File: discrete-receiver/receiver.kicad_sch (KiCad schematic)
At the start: 75 parts, among them J1 His Excellence, J7 Her Excellency, T1 H1102NLT, T2 MABA-007159-000000, U1 SN74CBT3253DBQR, U16 PSA4-5043_, U18 SN74LVC1G3157DBVR, U2 OPA1612AxD, U3 OPA1612AxD, U5 ADE-12+

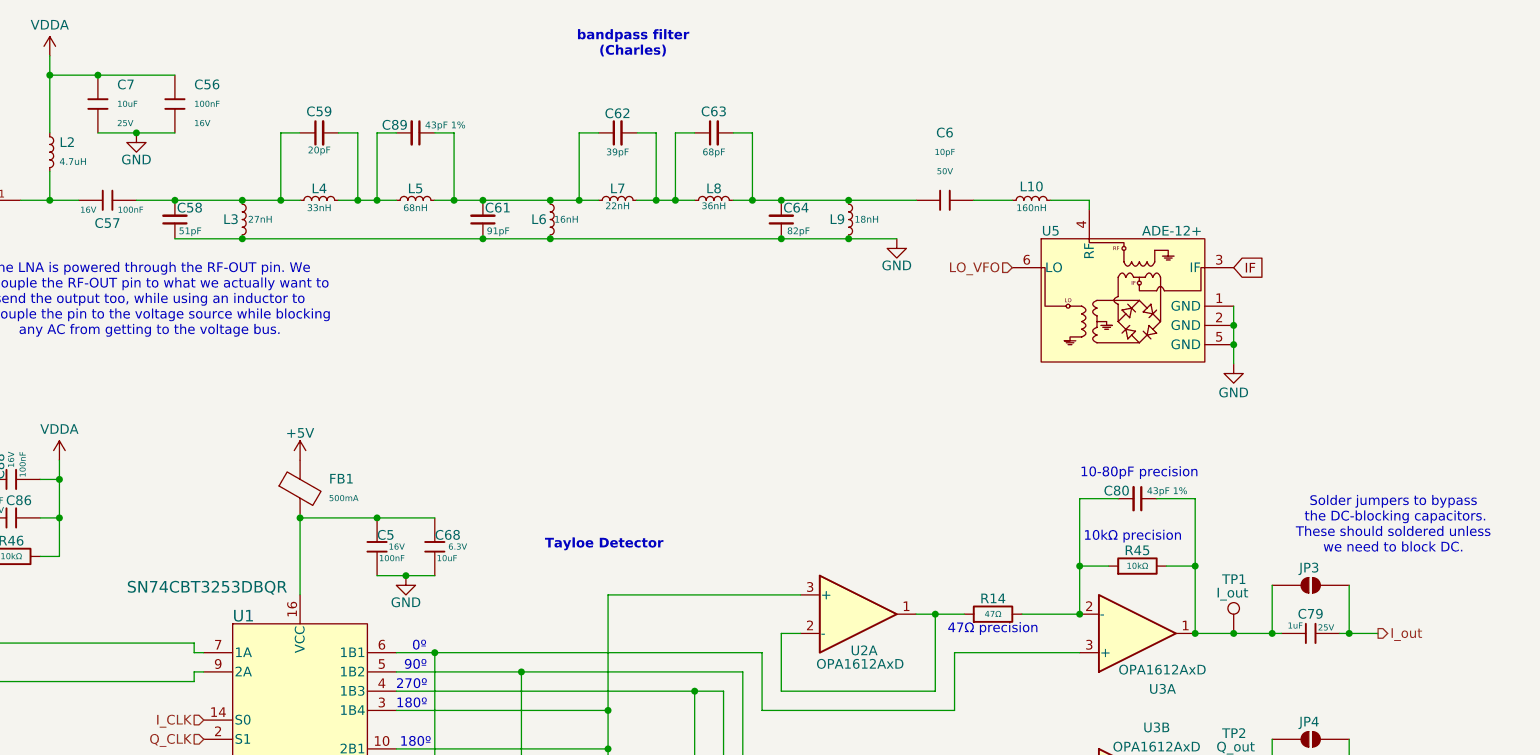
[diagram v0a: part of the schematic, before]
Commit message: Added Charles Mux
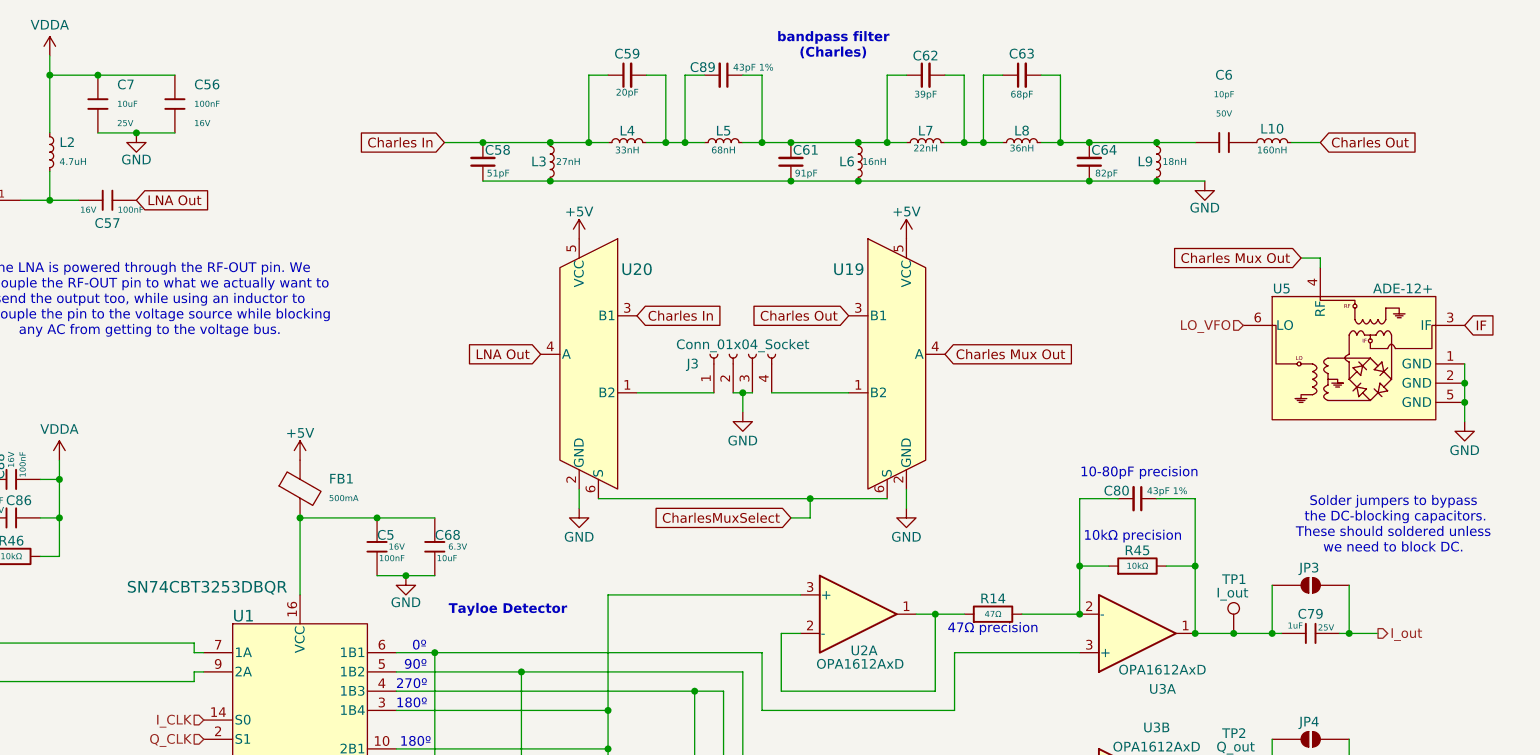
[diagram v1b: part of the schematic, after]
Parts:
- added J3: Conn_01x04_Socket, symbol Connector:Conn_01x04_Socket
- added U19, U20: SN74LVC1G3157DBVR, DBV6, symbol sdr_project:SN74LVC1G3157DBVR
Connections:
- net +5V: now also U19.5 (VCC), U20.5 (VCC)
- net GND: now also J3.2 (Pin_2), J3.3 (Pin_3), U19.2 (GND), U20.2 (GND)
- net Charles In: now reaches C58.2, C59.1, L3.1, L4.1
- net Charles In: now also U20.3 (B1); no longer C57.2
- net Charles Mux Out: now reaches U5.4 (RF)
- net Charles Mux Out: now also U19.4 (A); no longer L10.2
- new net: J3.1 (Pin_1), U20.1 (B2)
- new net: J3.4 (Pin_4), U19.1 (B2)
- new net Charles Out: L10.2, U19.3 (B1)
- new net CharlesMuxSelect: U19.6 (S), U20.6 (S)
- new net LNA Out: C57.2, U20.4 (A)

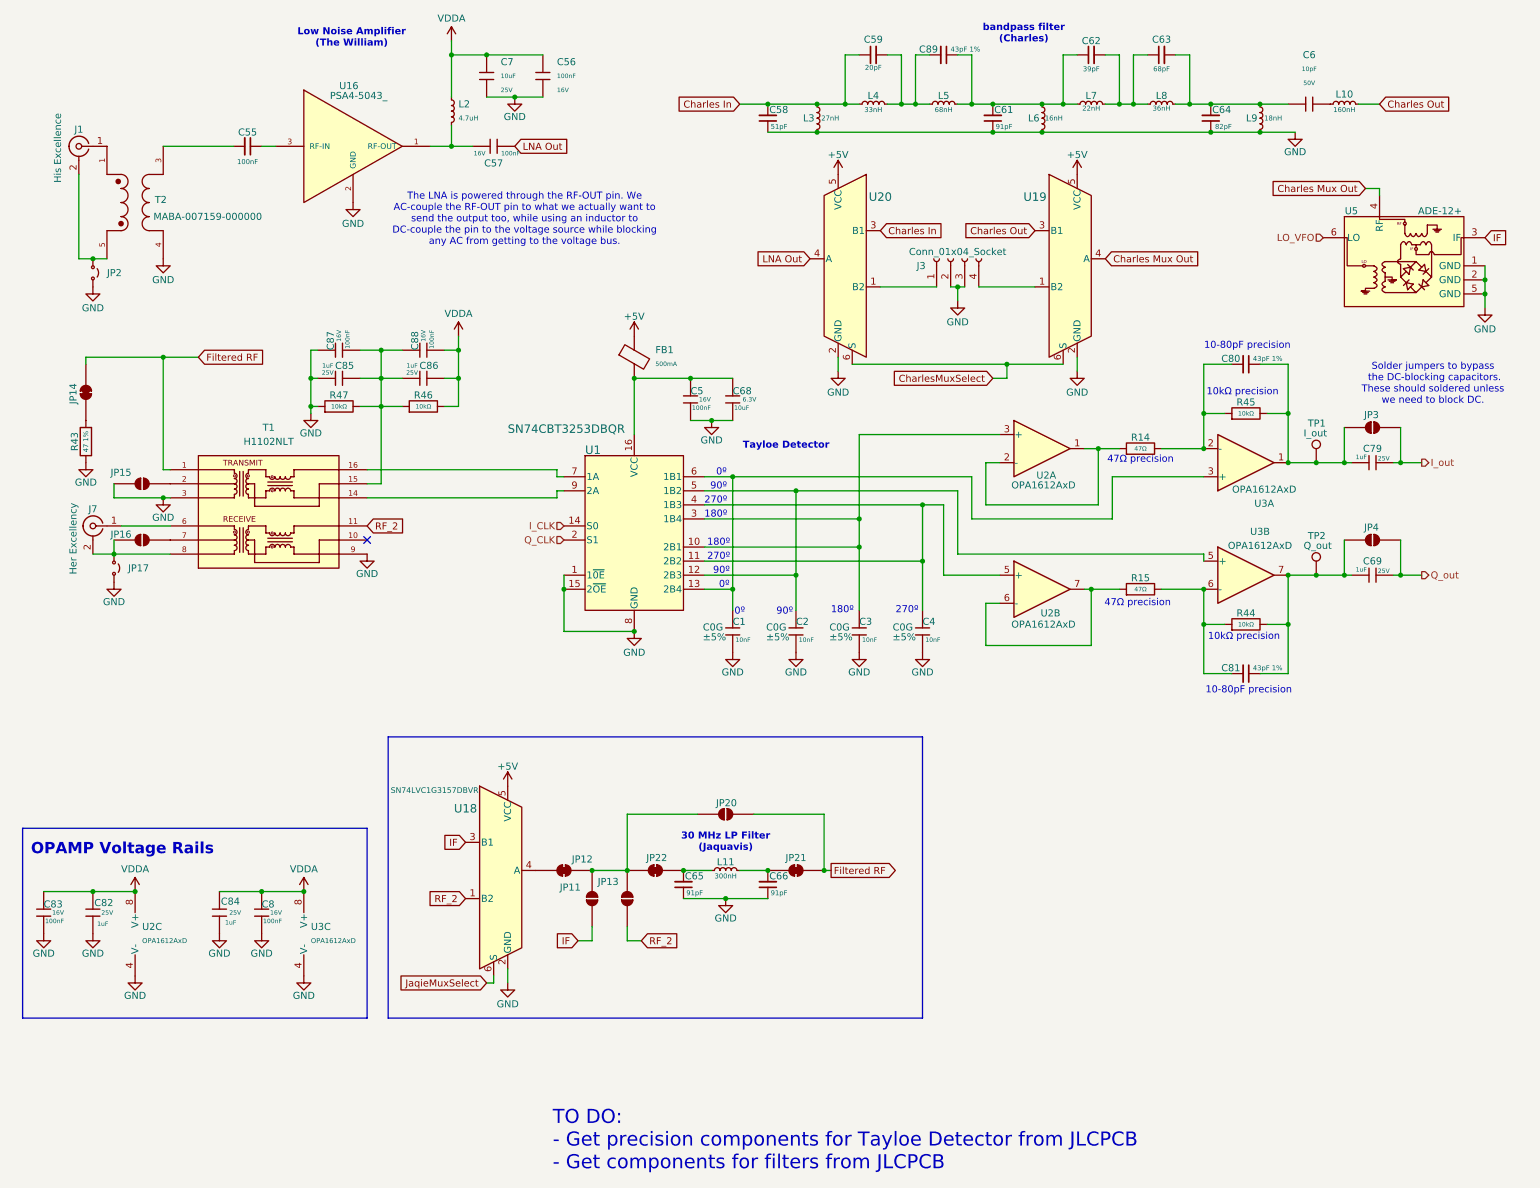
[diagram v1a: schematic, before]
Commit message: Created Tayloe Detector Subsheet
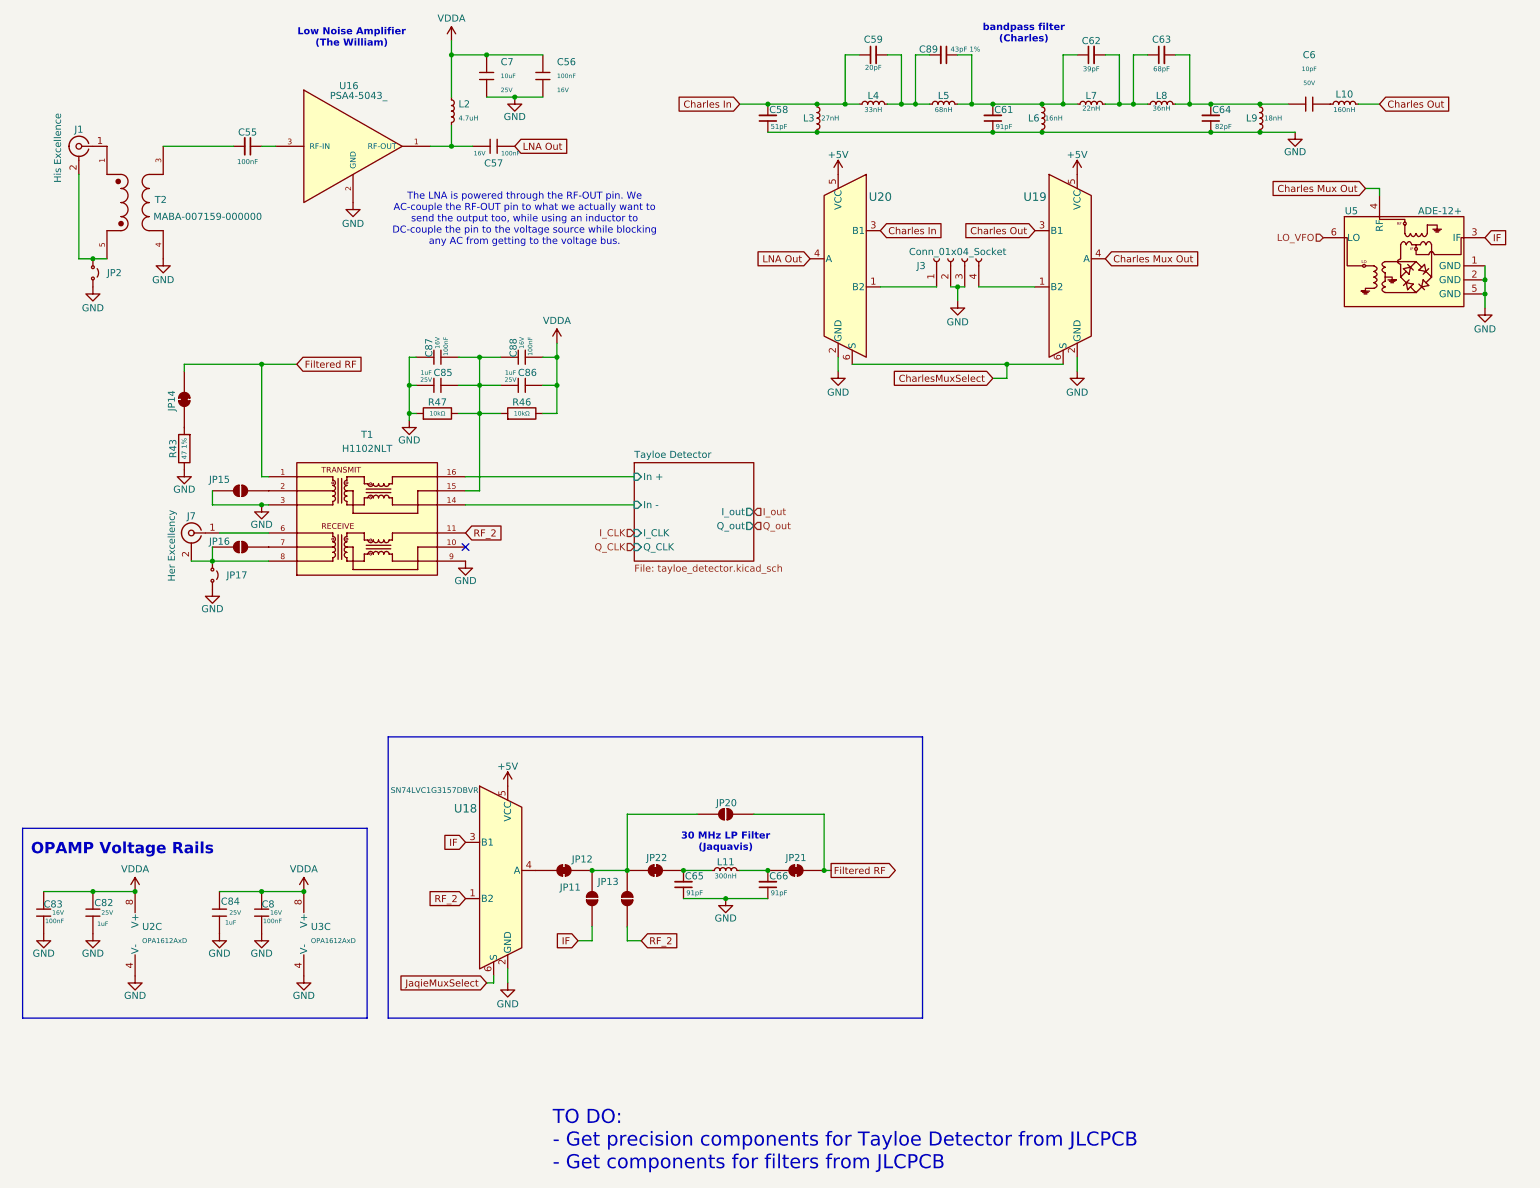
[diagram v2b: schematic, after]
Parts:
- removed C1, C2, C3, C4: 10nF, PCM_JLCPCB:C_0603, symbol PCM_JLCPCB-Capacitors:0603,330pF
- removed C5: 100nF, PCM_JLCPCB:C_0402, symbol PCM_JLCPCB-Capacitors:0402,100nF
- removed C68: 10uF, PCM_JLCPCB:C_0402, symbol PCM_JLCPCB-Capacitors:0402,10uF
- removed C69, C79: 1uF, PCM_JLCPCB:C_0402, symbol PCM_JLCPCB-Capacitors:0402,1uF
- removed C80, C81: 43pF 1%, symbol Device:C_Small
- removed FB1: (no value), PCM_JLCPCB:FB_0805, symbol PCM_JLCPCB-Inductors:Ferrite,0805,(2)
- removed JP3, JP4: SolderJumper_2_Open, symbol Jumper:SolderJumper_2_Open
- removed R14, R15: 47Ω, PCM_JLCPCB:R_0402, symbol PCM_JLCPCB-Resistors:0402,47Ω
- removed R44, R45: 10kΩ, PCM_JLCPCB:R_0402, symbol PCM_JLCPCB-Resistors:0402,10kΩ
- removed TP1: I_out, symbol Connector:TestPoint
- removed TP2: Q_out, symbol Connector:TestPoint
- removed U1: SN74CBT3253DBQR, DBQ16, symbol sdr_project:SN74CBT3253DBQR
- removed unit 2 of U2
- removed unit 1 of U2
- removed unit 2 of U3
- removed unit 1 of U3
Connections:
- net Tayloe Detector/In -: now reaches T1.14
- net Tayloe Detector/In +: now reaches T1.16
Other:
- added sheet Tayloe Detector (tayloe_detector.kicad_sch)
- note removed: "0º"
- note removed: "10-80pF precision"
- note removed: "10kΩ precision"
- note removed: "180º"
- note removed: "270º"
- note removed: "47Ω precision"
- note removed: "90º"
- note removed: "Solder jumpers to bypass the DC-blocking capacitors. These should soldered unless we need to block DC."
- note removed: "Tayloe Detector"

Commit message: Created subsheet for Charles
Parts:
- removed C58: 51pF, symbol Device:C_Small
- removed C59: 20pF, symbol Device:C_Small
- removed C6: 10pF, PCM_JLCPCB:C_0402, symbol PCM_JLCPCB-Capacitors:0402,10pF
- removed C61: 91pF, symbol Device:C_Small
- removed C62: 39pF, symbol Device:C_Small
- removed C63: 68pF, symbol Device:C_Small
- removed C64: 82pF, symbol Device:C_Small
- removed C89: 43pF 1%, symbol Device:C_Small
- removed L10: 160nH, symbol Device:L_Small
- removed L3: 27nH, symbol Device:L_Small
- removed L4: 33nH, symbol Device:L_Small
- removed L5: 68nH, symbol Device:L_Small
- removed L6: 16nH, symbol Device:L_Small
- removed L7: 22nH, symbol Device:L_Small
- removed L8: 36nH, symbol Device:L_Small
- removed L9: 18nH, symbol Device:L_Small
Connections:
- net Charles In renamed Charles/RF In
- net Charles Mux Out renamed VHF BP Filter Mux Out
- net Charles Out renamed Charles/RF Out
- net CharlesMuxSelect renamed VHF BP Filter Mux Select
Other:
- added sheet Charles (charles.kicad_sch)
- note removed: "bandpass filter (Charles)"
- moved on the sheet: J3
